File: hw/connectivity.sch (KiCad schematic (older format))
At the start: 113 parts, among them P1 CONN_13X3, P10 MICROSD, P11 CONN_9, P12 CONN_2, P13 CONN_6, P19 CONN_1, P2 CONN_4, P20 CONN_1, P21 CONN_1, P22 CONN_1, P3 CONN_4, P4 MICROUSB, P5 CONN_4, P6 CONN_6, P7 CONN_4, P8 CONN_4, P9 CONN_4, Q1 PDTC114EE, Q2 PDTC114EE, Q3 PDTA114YE, Q4 PDTC114EE, Q5 PDTC114EE, Q6 PDTC114EE, Q7 PDTC114EE, SW1 STG719, U1 XBEE, U2 LTC4411, U3 SN65HVD233, U4 ADP3338AKCZ-3.3, U5 LT1761-3.3, U6 EL1883

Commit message: schematic: BJTs in S.BUS and S.PORT inverters replaced by MOSFETs (faster switching speed)
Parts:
- removed Q1, Q2: PDTC114EE, sc75, symbol PDTC114EE
- removed Q3: PDTA114YE, sc75, symbol PDTA114YE
- added Q1, Q2: NTA4153NT1G, ~, symbol NTA4153NT1G
- added Q3: NTA4151PT1G, ~, symbol NTA4151PT1G
- added R66, R67: 39k, r_0603, symbol R
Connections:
- wire segments 294 -> 299
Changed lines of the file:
@@
 Sheet 2 3
 Title "DRACO - connectivity sheet"
-Date "28 dec 2013"
+Date "26 jan 2014"
 Rev "0.9"
 Comp "dandys"
@@
 L GND #PWR011
 U 1 1 524DB3D2
-P 2600 4800
-F 0 "#PWR011" H 2600 4800 30  0001 C CNN
-F 1 "GND" H 2600 4730 30  0000 C CNN
-F 2 "" H 2600 4800 60  0000 C CNN
-F 3 "" H 2600 4800 60  0000 C CNN
-	1    2600 4800
-	1    0    0    -1
-$EndComp
-Wire Wire Line
-	1300 4500 2200 4500
+P 2100 5100
+F 0 "#PWR011" H 2100 5100 30  0001 C CNN
+F 1 "GND" H 2200 5050 30  0000 C CNN
+F 2 "" H 2100 5100 60  0000 C CNN
+F 3 "" H 2100 5100 60  0000 C CNN
+	1    2100 5100
+	1    0    0    -1
+$EndComp
+Wire Wire Line
+	1300 4500 2300 4500
 Text GLabel 2750 4200 2    60   Output ~ 0
 SBUS
@@
 Connection ~ 11200 1300
 $Comp
-L PDTC114EE Q1
-U 1 1 5250105C
-P 2500 4500
-F 0 "Q1" H 2750 4600 50  0000 R CNN
-F 1 "PDTC114EE" H 3100 4400 50  0000 R CNN
-F 2 "sc75" H 2500 4500 60  0001 C CNN
-F 3 "~" H 2500 4500 60  0000 C CNN
-	1    2500 4500
-	1    0    0    -1
-$EndComp
-Wire Wire Line
-	2600 4750 2600 4800
-$Comp
 L R R18
 U 1 1 52501265
@@
 $EndComp
 Wire Wire Line
-	2600 4200 2600 4250
+	2600 4200 2600 4300
 Wire Wire Line
 	2600 3650 2600 3700
@@
 S.PORT / S.BUS 2.0
 $Comp
-L PDTC114EE Q2
-U 1 1 52502569
-P 13900 6100
-F 0 "Q2" H 14150 6200 50  0000 R CNN
-F 1 "PDTC114EE" H 13900 6350 50  0000 R CNN
-F 2 "sc75" H 13900 6100 60  0001 C CNN
-F 3 "~" H 13900 6100 60  0000 C CNN
-	1    13900 6100
-	-1   0    0    -1
-$EndComp
-$Comp
 L R R44
 U 1 1 52502676
@@
 $EndComp
 Wire Wire Line
-	13800 6350 13800 6400
+	13800 6300 13800 6400
 Text GLabel 13700 5800 0    60   Output ~ 0
 SPORT_RX
 Wire Wire Line
-	13800 5850 13800 5750
+	13800 5750 13800 5900
 Wire Wire Line
 	13800 5250 13800 5200
@@
 	13700 5800 13800 5800
 Connection ~ 13800 5800
-$Comp
-L PDTA114YE Q3
-U 1 1 52502E4B
-P 14150 6750
-F 0 "Q3" H 14450 6850 60  0000 R CNN
-F 1 "PDTA114YE" H 13950 6900 60  0000 R CNN
-F 2 "sc75" H 14150 6750 60  0001 C CNN
-F 3 "~" H 14150 6750 60  0000 C CNN
-	1    14150 6750
-	1    0    0    -1
-$EndComp
-Wire Wire Line
-	14200 6100 14300 6100
-Wire Wire Line
-	14250 6100 14250 6500
+Wire Wire Line
+	14100 6100 14300 6100
+Wire Wire Line
+	14250 6100 14250 6550
 Connection ~ 14250 6100
 Wire Wire Line
-	14250 7000 14250 7100
+	14250 6950 14250 7100
 Wire Wire Line
 	14250 7100 14500 7100
-Wire Wire Line
-	14500 7100 14500 6900
 $Comp
 L +3.3V #PWR040
 U 1 1 52503155
-P 14500 6900
-F 0 "#PWR040" H 14500 6860 30  0001 C CNN
-F 1 "+3.3V" H 14500 7010 30  0000 C CNN
-F 2 "" H 14500 6900 60  0000 C CNN
-F 3 "" H 14500 6900 60  0000 C CNN
-	1    14500 6900
+P 14500 7000
+F 0 "#PWR040" H 14500 6960 30  0001 C CNN
+F 1 "+3.3V" H 14500 7110 30  0000 C CNN
+F 2 "" H 14500 7000 60  0000 C CNN
+F 3 "" H 14500 7000 60  0000 C CNN
+	1    14500 7000
 	1    0    0    -1
 $EndComp
@@
 SPORT_TX
 Wire Wire Line
-	13750 6750 13850 6750
+	13750 6750 13950 6750
 $Comp
 L R R25
@@
 Wire Wire Line
 	15200 4300 15300 4300
+$Comp
+L NTA4153NT1G Q1
+U 1 1 52E51B81
+P 2500 4500
+F 0 "Q1" H 2510 4670 60  0000 R CNN
+F 1 "NTA4153NT1G" H 3250 4500 60  0000 R CNN
+F 2 "~" H 2500 4500 60  0000 C CNN
+F 3 "~" H 2500 4500 60  0000 C CNN
+	1    2500 4500
+	1    0    0    -1
+$EndComp
+$Comp
+L R R66
+U 1 1 52E5201C
+P 2100 4800
+F 0 "R66" V 2200 4900 40  0000 C CNN
+F 1 "39k" V 2100 4800 40  0000 C CNN
+F 2 "r_0603" V 2030 4800 30  0001 C CNN
+F 3 "~" H 2100 4800 30  0000 C CNN
+	1    2100 4800
+	-1   0    0    1
+$EndComp
+Wire Wire Line
+	2100 4550 2100 4500
+Connection ~ 2100 4500
+Wire Wire Line
+	2100 5050 2600 5050
+Wire Wire Line
+	2100 5050 2100 5100
+Wire Wire Line
+	2600 5050 2600 4700
+$Comp
+L NTA4153NT1G Q2
+U 1 1 52E529B2
+P 13900 6100
+F 0 "Q2" H 13910 6270 60  0000 R CNN
+F 1 "NTA4153NT1G" H 14650 6100 60  0000 R CNN
+F 2 "~" H 13900 6100 60  0000 C CNN
+F 3 "~" H 13900 6100 60  0000 C CNN
+	1    13900 6100
+	-1   0    0    -1
+$EndComp
+$Comp
+L R R67
+U 1 1 52E52E48
+P 14550 6300
+F 0 "R67" V 14650 6400 40  0000 C CNN
+F 1 "39k" V 14550 6300 40  0000 C CNN
+F 2 "r_0603" V 14480 6300 30  0001 C CNN
+F 3 "~" H 14550 6300 30  0000 C CNN
+	1    14550 6300
+	0    -1   -1   0
+$EndComp
+Wire Wire Line
+	14250 6300 14300 6300
+Connection ~ 14250 6300
+Wire Wire Line
+	14800 6300 14850 6300
+$Comp
+L NTA4151PT1G Q3
+U 1 1 52E53470
+P 14150 6750
+F 0 "Q3" H 14150 6940 60  0000 R CNN
+F 1 "NTA4151PT1G" H 14900 6750 60  0000 R CNN
+F 2 "~" H 14150 6750 60  0000 C CNN
+F 3 "~" H 14150 6750 60  0000 C CNN
+	1    14150 6750
+	1    0    0    -1
+$EndComp
+Wire Wire Line
+	14500 7100 14500 7000
 $EndSCHEMATC

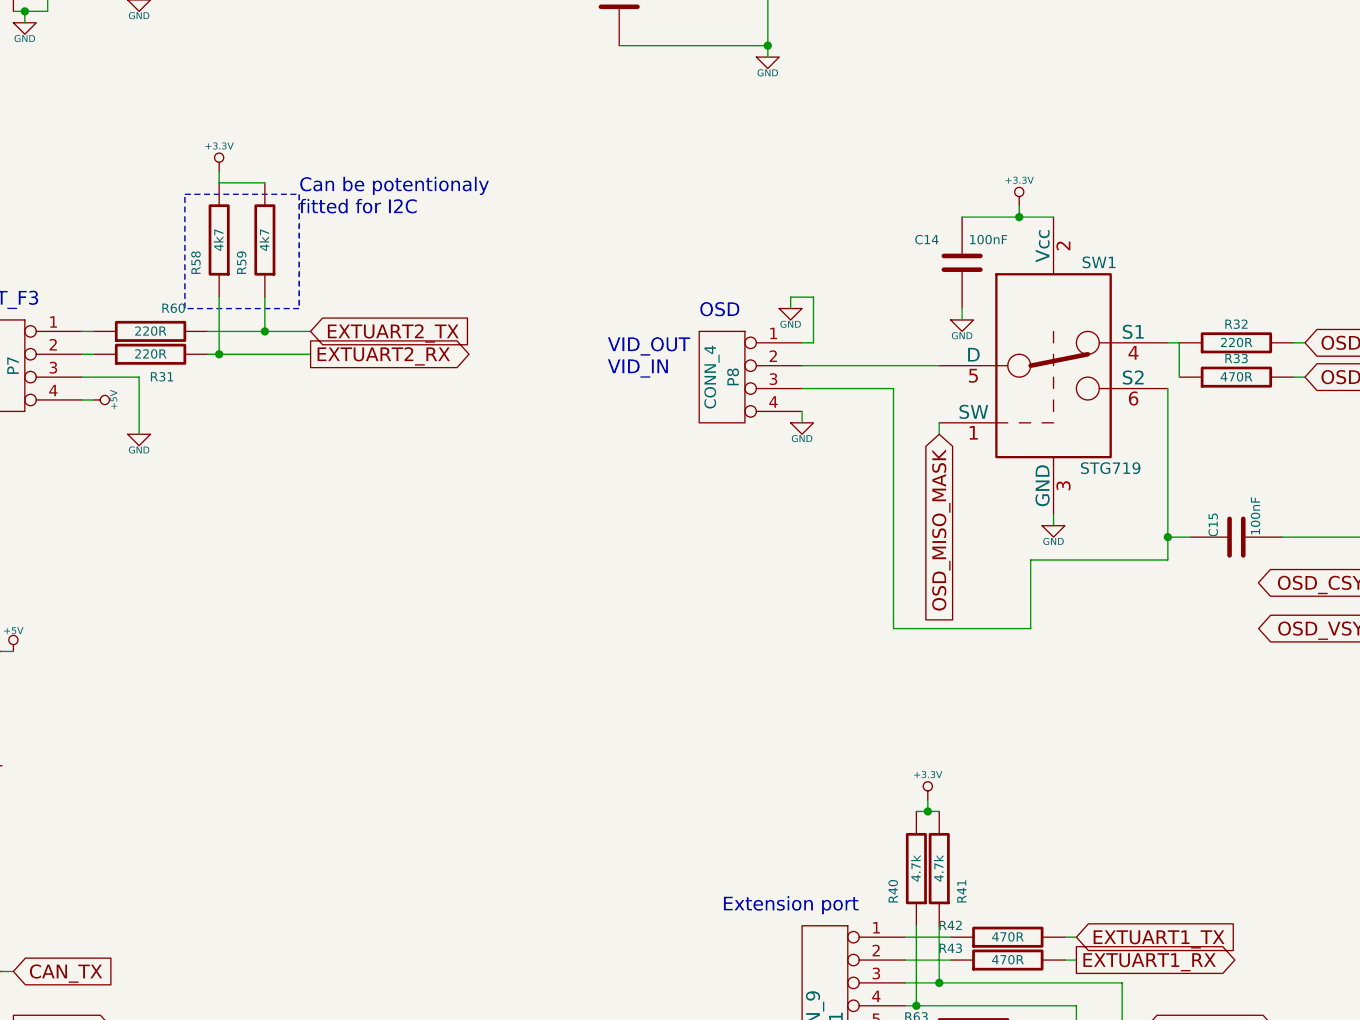
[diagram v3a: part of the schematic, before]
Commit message: schematics: preparations for board rev. 1.0 MPU-6000 and HMC5893 replaced by single chip solution MPU-9250 Added video sync tip clamping MAX4090
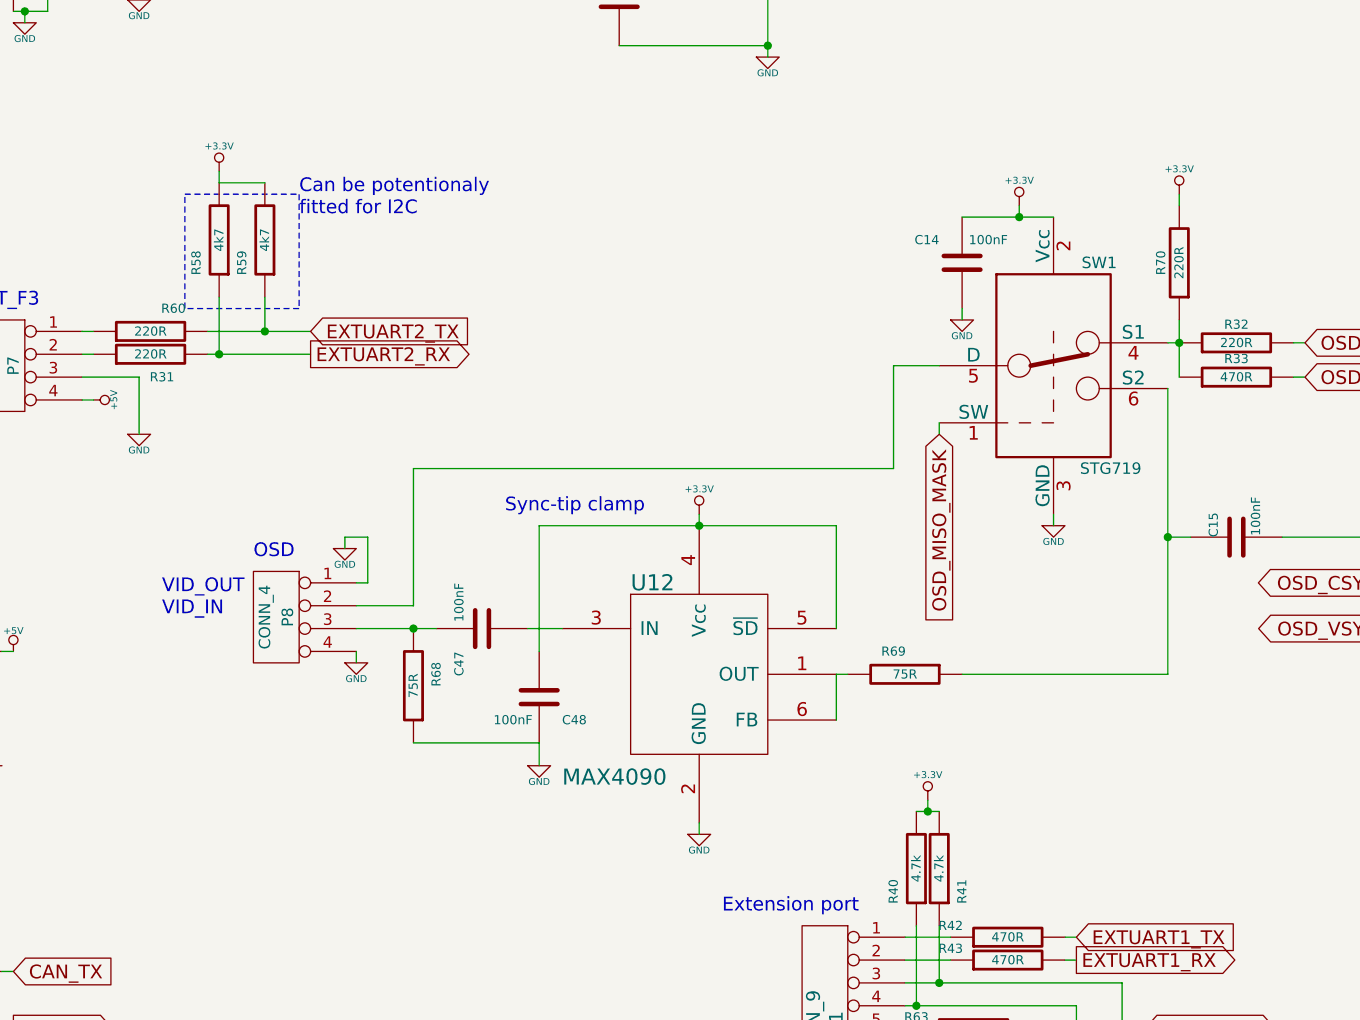
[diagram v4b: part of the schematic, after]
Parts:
- added C47, C48: 100nF, c_0603, symbol C
- added R68, R69: 75R, r_0603, symbol R
- added R70: 220R, r_0603, symbol R
- added U12: MAX4090, ~, symbol MAX4090
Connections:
- wire segments 299 -> 311
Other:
- note added: "Sync-tip clamp"
- moved on the sheet: P8
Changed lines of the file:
@@
 Sheet 2 3
 Title "DRACO - connectivity sheet"
-Date "11 feb 2014"
-Rev "0.9"
+Date "15 feb 2014"
+Rev "1.0"
 Comp "dandys"
 Comment1 ""
@@
 L CONN_4 P8
 U 1 1 525440A0
-P 6950 4400
-F 0 "P8" V 6900 4400 50  0000 C CNN
-F 1 "CONN_4" V 7000 4400 50  0000 C CNN
-F 2 "picoblade_4-90" H 6950 4400 60  0001 C CNN
-F 3 "~" H 6950 4400 60  0000 C CNN
-	1    6950 4400
+P 5000 5450
+F 0 "P8" V 4950 5450 50  0000 C CNN
+F 1 "CONN_4" V 5050 5450 50  0000 C CNN
+F 2 "picoblade_4-90" H 5000 5450 60  0001 C CNN
+F 3 "~" H 5000 5450 60  0000 C CNN
+	1    5000 5450
 	-1   0    0    -1
 $EndComp
@@
 L GND #PWR047
 U 1 1 525440CE
-P 7300 4600
-F 0 "#PWR047" H 7300 4600 30  0001 C CNN
-F 1 "GND" H 7300 4530 30  0000 C CNN
-F 2 "" H 7300 4600 60  0000 C CNN
-F 3 "" H 7300 4600 60  0000 C CNN
-	1    7300 4600
-	1    0    0    -1
-$EndComp
-Wire Wire Line
-	7300 4550 7300 4600
+P 5350 5650
+F 0 "#PWR047" H 5350 5650 30  0001 C CNN
+F 1 "GND" H 5350 5580 30  0000 C CNN
+F 2 "" H 5350 5650 60  0000 C CNN
+F 3 "" H 5350 5650 60  0000 C CNN
+	1    5350 5650
+	1    0    0    -1
+$EndComp
+Wire Wire Line
+	5350 5600 5350 5650
 $Comp
 L GND #PWR048
 U 1 1 525441DB
-P 7250 4100
-F 0 "#PWR048" H 7250 4100 30  0001 C CNN
-F 1 "GND" H 7250 4030 30  0000 C CNN
-F 2 "" H 7250 4100 60  0000 C CNN
-F 3 "" H 7250 4100 60  0000 C CNN
-	1    7250 4100
-	1    0    0    -1
-$EndComp
-Wire Wire Line
-	7300 4250 7350 4250
-Wire Wire Line
-	7350 4250 7350 4050
-Wire Wire Line
-	7350 4050 7250 4050
-Wire Wire Line
-	7250 4050 7250 4100
-Wire Wire Line
-	7300 4350 7900 4350
+P 5300 5150
+F 0 "#PWR048" H 5300 5150 30  0001 C CNN
+F 1 "GND" H 5300 5080 30  0000 C CNN
+F 2 "" H 5300 5150 60  0000 C CNN
+F 3 "" H 5300 5150 60  0000 C CNN
+	1    5300 5150
+	1    0    0    -1
+$EndComp
+Wire Wire Line
+	5350 5300 5400 5300
+Wire Wire Line
+	5400 5300 5400 5100
+Wire Wire Line
+	5400 5100 5300 5100
+Wire Wire Line
+	5300 5100 5300 5150
 Text GLabel 7900 4650 3    60   Input ~ 0
 OSD_MISO_MASK
@@
 	8250 3650 8250 3700
 Connection ~ 8250 3700
-Wire Wire Line
-	7300 4450 7700 4450
-Wire Wire Line
-	7700 4450 7700 5500
-Wire Wire Line
-	7700 5500 8300 5500
-Wire Wire Line
-	8300 5500 8300 5200
-Wire Wire Line
-	8300 5200 8900 5200
-Wire Wire Line
-	8900 5200 8900 4450
 $Comp
 L R R32
@@
 $EndComp
 Wire Wire Line
-	8950 4400 8950 4250
+	8950 4150 8950 4400
 Wire Wire Line
 	8950 4250 8900 4250
@@
 Wire Wire Line
 	8900 5100 9000 5100
-Connection ~ 8900 5100
 Wire Wire Line
 	9400 5100 9950 5100
@@
 Wire Wire Line
 	9900 5500 9950 5500
-Text Notes 6850 4150 0    60   ~ 0
+Text Notes 4900 5200 0    60   ~ 0
 OSD
-Text Notes 6450 4400 0    60   ~ 0
+Text Notes 4500 5450 0    60   ~ 0
 VID_OUT\nVID_IN
 $Comp
@@
 Wire Wire Line
 	14500 7100 14500 7000
+$Comp
+L MAX4090 U12
+U 1 1 52FFBE54
+P 6850 5700
+F 0 "U12" H 6550 6100 70  0000 L CNN
+F 1 "MAX4090" H 6250 5250 70  0000 L CNN
+F 2 "~" H 6600 5700 60  0000 C CNN
+F 3 "~" H 6600 5700 60  0000 C CNN
+	1    6850 5700
+	1    0    0    -1
+$EndComp
+$Comp
+L GND #PWR062
+U 1 1 52FFBE61
+P 6850 6400
+F 0 "#PWR062" H 6850 6400 30  0001 C CNN
+F 1 "GND" H 6850 6330 30  0000 C CNN
+F 2 "" H 6850 6400 60  0000 C CNN
+F 3 "" H 6850 6400 60  0000 C CNN
+	1    6850 6400
+	1    0    0    -1
+$EndComp
+Wire Wire Line
+	6850 6350 6850 6400
+$Comp
+L C C47
+U 1 1 52FFBFE7
+P 5900 5500
+F 0 "C47" H 6000 5400 40  0000 L CNN
+F 1 "100nF" H 5700 5400 40  0000 L CNN
+F 2 "c_0603" H 5938 5350 30  0001 C CNN
+F 3 "~" H 5900 5500 60  0000 C CNN
+	1    5900 5500
+	0    1    1    0
+$EndComp
+Wire Wire Line
+	6100 5500 6250 5500
+$Comp
+L R R68
+U 1 1 52FFC16E
+P 5600 5750
+F 0 "R68" V 5500 5700 40  0000 C CNN
+F 1 "75R" V 5600 5750 40  0000 C CNN
+F 2 "r_0603" V 5530 5750 30  0001 C CNN
+F 3 "~" H 5600 5750 30  0000 C CNN
+	1    5600 5750
+	-1   0    0    1
+$EndComp
+Wire Wire Line
+	5350 5500 5700 5500
+$Comp
+L C C48
+U 1 1 52FFC929
+P 6150 5800
+F 0 "C48" H 6250 5700 40  0000 L CNN
+F 1 "100nF" H 5950 5700 40  0000 L CNN
+F 2 "c_0603" H 6188 5650 30  0001 C CNN
+F 3 "~" H 6150 5800 60  0000 C CNN
+	1    6150 5800
+	1    0    0    -1
+$EndComp
+Wire Wire Line
+	6150 5600 6150 5050
+Wire Wire Line
+	6150 5050 7450 5050
+$Comp
+L +3.3V #PWR063
+U 1 1 52FFCAB2
+P 6850 5000
+F 0 "#PWR063" H 6850 4960 30  0001 C CNN
+F 1 "+3.3V" H 6850 5110 30  0000 C CNN
+F 2 "" H 6850 5000 60  0000 C CNN
+F 3 "" H 6850 5000 60  0000 C CNN
+	1    6850 5000
+	1    0    0    -1
+$EndComp
+Wire Wire Line
+	6850 5050 6850 5000
+Wire Wire Line
+	6150 6000 5600 6000
+$Comp
+L GND #PWR064
+U 1 1 52FFCDC3
+P 6150 6100
+F 0 "#PWR064" H 6150 6100 30  0001 C CNN
+F 1 "GND" H 6150 6030 30  0000 C CNN
+F 2 "" H 6150 6100 60  0000 C CNN
+F 3 "" H 6150 6100 60  0000 C CNN
+	1    6150 6100
+	1    0    0    -1
+$EndComp
+Wire Wire Line
+	6150 6000 6150 6100
+Wire Wire Line
+	7450 5900 7450 5700
+Wire Wire Line
+	7450 5050 7450 5500
+Connection ~ 6850 5050
+$Comp
+L R R69
+U 1 1 52FFD3E8
+P 7750 5700
+F 0 "R69" V 7650 5650 40  0000 C CNN
+F 1 "75R" V 7750 5700 40  0000 C CNN
+F 2 "r_0603" V 7680 5700 30  0001 C CNN
+F 3 "~" H 7750 5700 30  0000 C CNN
+	1    7750 5700
+	0    1    1    0
+$EndComp
+Wire Wire Line
+	7450 5700 7500 5700
+Text Notes 6000 5000 0    60   ~ 0
+Sync-tip clamp
+Wire Wire Line
+	8900 4450 8900 5700
+Wire Wire Line
+	8900 5700 8000 5700
+Connection ~ 8900 5100
+Connection ~ 5600 5500
+Wire Wire Line
+	7900 4350 7700 4350
+Wire Wire Line
+	7700 4350 7700 4800
+Wire Wire Line
+	7700 4800 5600 4800
+Wire Wire Line
+	5600 4800 5600 5400
+Wire Wire Line
+	5600 5400 5350 5400
+$Comp
+L R R70
+U 1 1 52FFE4FA
+P 8950 3900
+F 0 "R70" V 9030 3900 40  0000 C CNN
+F 1 "220R" V 8950 3900 40  0000 C CNN
+F 2 "r_0603" V 8880 3900 30  0001 C CNN
+F 3 "~" H 8950 3900 30  0000 C CNN
+	1    8950 3900
+	-1   0    0    1
+$EndComp
+Connection ~ 8950 4250
+$Comp
+L +3.3V #PWR065
+U 1 1 52FFE68D
+P 8950 3600
+F 0 "#PWR065" H 8950 3560 30  0001 C CNN
+F 1 "+3.3V" H 8950 3710 30  0000 C CNN
+F 2 "" H 8950 3600 60  0000 C CNN
+F 3 "" H 8950 3600 60  0000 C CNN
+	1    8950 3600
+	1    0    0    -1
+$EndComp
+Wire Wire Line
+	8950 3600 8950 3650
 $EndSCHEMATC

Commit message: HW board revision 1.0
- HMC5983 and MPU6000 replaced by MPU9250 on SPI bus
- added video sync-tip clamping and buffer circuit MAX4090
- added shottky diode D1 as optional alternative for ideal diode circuit LTC4411
- SPI pixel clock generation now also connected to timer output for more fine clock tuning to be possible
- PWM11 and PWM12 signals now switched to PD12 and PD13 to avoid collision of timer usage for sonar echo measurement
- SMT32F4 LEDs moved to more suitable place on the board and blue LED switched to GPIO PC5 (was PE3)
- added micro button
- SWD pads for STM32F3 is now standard 2.54 pitch header
- added SPI flash MICRON N25Q032A13ESC40G
- added pulldown resistors for Q1, Q2
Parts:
- added D1: PMEG6010CEH, ~, symbol DIODESCH
- added G1, G2, G3, G4, G5: DUMMY, ~, symbol DUMMY
- R70: value 220R -> 390R
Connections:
- wire segments 311 -> 315
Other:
- note added: "LTC1411 alternative"
- note added: "Mechanical mount holes\nand drawings"
- note removed: "Mechanical mount holes"
